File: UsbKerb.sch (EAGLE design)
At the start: 8 parts, among them IC1 XMEGA16A4A

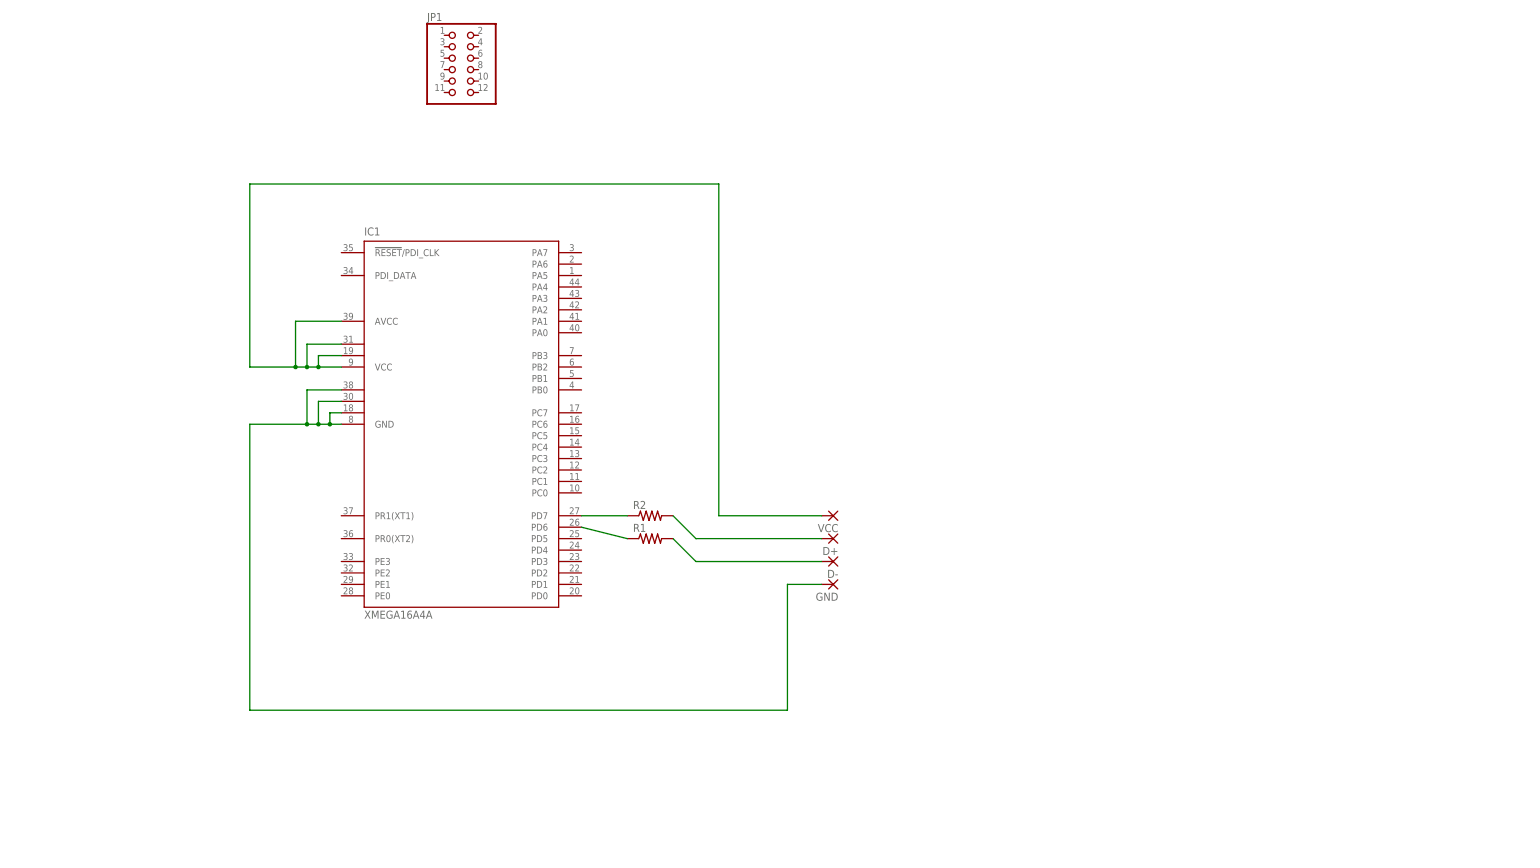
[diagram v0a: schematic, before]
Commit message: more footprints added
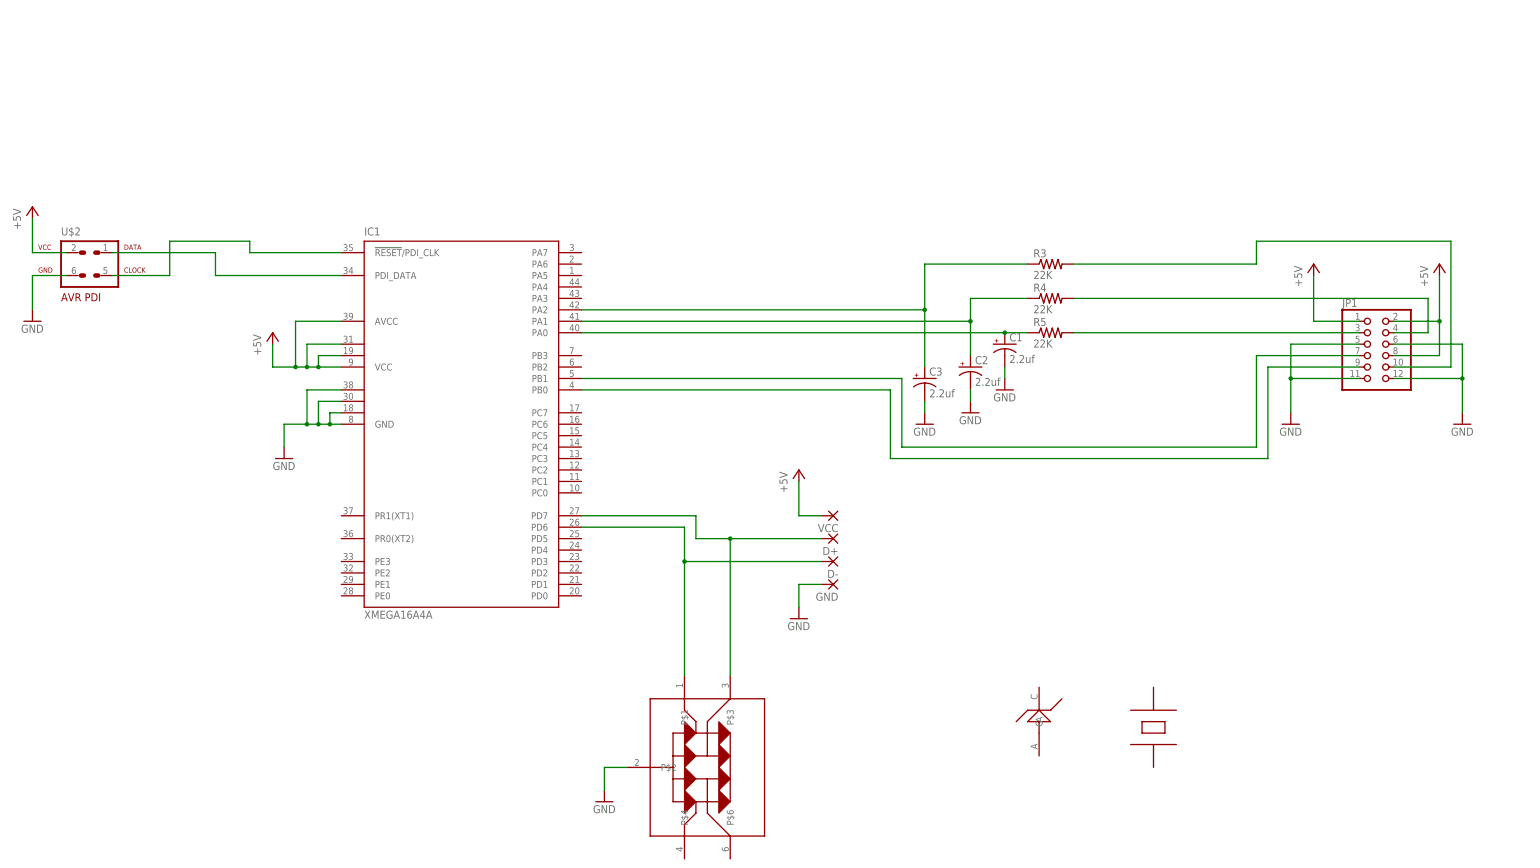
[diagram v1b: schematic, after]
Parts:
- removed R1, R2: (no value), resistor:R-US_R0805W
- added C1, C2, C3: 2.2uf, resistor:CPOL-USB
- added R3, R4, R5: 22K, resistor:R-US_R0805W
- added U$1: PUSB2X4Y, usb:PUSB2X4Y
- added U$2: AVR-PDIVERT, avr-7:AVR-PDIVERT
- added U$3: TVS, usb:TVS
- added U$4: 12MHZ, usb:12MHZ
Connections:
- new net +5V: IC1.AVCC, IC1.VCC, IC1.VCC1, IC1.VCC2, JP1.1, JP1.2, JP1.8, U$2.2, VCC.P
- new net GND: C1.-, C2.-, C3.-, GND.P, IC1.GND, IC1.GND1, IC1.GND2, IC1.GND3, JP1.11, JP1.12, JP1.5, JP1.6, U$1.P$2, U$2.6
- new net N$10: JP1.3, R5.2
- new net N$11: IC1.PB0, JP1.9
- new net N$12: IC1.PB1, JP1.7
- new net N$6: C3.+, IC1.PA2, R3.1
- new net N$7: IC1.!RESET!/PDI_CLK, U$2.5
- new net N$9: JP1.4, R4.2
- net N$1: now also C1.+, IC1.PA0, R5.1; no longer IC1.PD6, R1.1
- net N$2: now also D+.P, U$1.P$3; no longer R2.1
- net N$3: now also IC1.PDI_DATA, U$2.1; no longer D+.P, R2.2
- net N$4: now also IC1.PD6, U$1.P$1; no longer R1.2
- net N$5: now also C2.+, IC1.PA1, R4.1; no longer IC1.AVCC, IC1.VCC, IC1.VCC1, IC1.VCC2, VCC.P
- net N$8: now also JP1.10, R3.2; no longer GND.P, IC1.GND, IC1.GND1, IC1.GND2, IC1.GND3
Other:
- moved on the sheet: JP1

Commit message: Replaced out of stock tvs foot print
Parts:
- U$1: value PUSB2X4Y -> 3.3TVS; device usb:PUSB2X4Y -> usb:3.3TVS
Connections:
- new net N$13: IC1.PR1(XT1), U$4.P$1
- new net N$14: IC1.PR0(XT2), U$4.P$2
- net +5V: now also U$1.VCC, U$3.C
- net GND: now also U$1.GND, U$3.A; no longer U$1.P$2
- net N$2: now also U$1.2; no longer U$1.P$3
- net N$4: now also U$1.1; no longer U$1.P$1
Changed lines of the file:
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@@
 <?xml version="1.0" encoding="utf-8"?>
 <!DOCTYPE eagle SYSTEM "eagle.dtd">
-<eagle version="7.1.0">
+<eagle version="7.2.0">
 <drawing>
 <settings>
@@
 <part name="C2" library="resistor" deviceset="CPOL-US" device="B" value="2.2uf"/>
 <part name="C3" library="resistor" deviceset="CPOL-US" device="B" value="2.2uf"/>
-<part name="U$1" library="usb" deviceset="PUSB2X4Y" device=""/>
 <part name="GND9" library="supply1" deviceset="GND" device=""/>
 <part name="U$2" library="avr-7" deviceset="AVR-PDI" device="VERT"/>
 <part name="U$3" library="usb" deviceset="TVS" device=""/>
 <part name="U$4" library="usb" deviceset="12MHZ" device=""/>
+<part name="U$1" library="usb" deviceset="3.3TVS" device=""/>
+<part name="P+6" library="supply1" deviceset="+5V" device=""/>
+<part name="P+7" library="supply1" deviceset="+5V" device=""/>
+<part name="GND10" library="supply1" deviceset="GND" device=""/>
 </parts>
 <sheets>
@@
 <instance part="C2" gate="G$1" x="180.34" y="63.5"/>
 <instance part="C3" gate="G$1" x="170.18" y="60.96"/>
-<instance part="U$1" gate="G$1" x="121.92" y="-25.4"/>
-<instance part="GND9" gate="1" x="99.06" y="-33.02"/>
+<instance part="GND9" gate="1" x="81.28" y="-33.02"/>
 <instance part="U$2" gate="G$1" x="-15.24" y="86.36"/>
 <instance part="U$3" gate="G$1" x="195.58" y="-15.24"/>
-<instance part="U$4" gate="G$1" x="220.98" y="-15.24" rot="R90"/>
+<instance part="U$4" gate="G$1" x="7.62" y="30.48" rot="R90"/>
+<instance part="U$1" gate="G$1" x="99.06" y="-22.86"/>
+<instance part="P+6" gate="1" x="81.28" y="-12.7"/>
+<instance part="P+7" gate="1" x="195.58" y="-2.54"/>
+<instance part="GND10" gate="1" x="195.58" y="-27.94"/>
 </instances>
 <busses>
@@
 <wire x1="119.38" y1="30.48" x2="119.38" y2="25.4" width="0.1524" layer="91"/>
 <wire x1="93.98" y1="30.48" x2="119.38" y2="30.48" width="0.1524" layer="91"/>
-<pinref part="U$1" gate="G$1" pin="P$3"/>
-<wire x1="127" y1="-5.08" x2="127" y2="25.4" width="0.1524" layer="91"/>
+<wire x1="127" y1="-20.32" x2="127" y2="25.4" width="0.1524" layer="91"/>
 <junction x="127" y="25.4"/>
+<pinref part="U$1" gate="G$1" pin="2"/>
+<wire x1="127" y1="-20.32" x2="111.76" y2="-20.32" width="0.1524" layer="91"/>
 </segment>
 </net>
@@
 <pinref part="IC1" gate="G$1" pin="PD6"/>
 <wire x1="116.84" y1="27.94" x2="93.98" y2="27.94" width="0.1524" layer="91"/>
-<pinref part="U$1" gate="G$1" pin="P$1"/>
-<wire x1="116.84" y1="-5.08" x2="116.84" y2="20.32" width="0.1524" layer="91"/>
+<wire x1="116.84" y1="-15.24" x2="116.84" y2="20.32" width="0.1524" layer="91"/>
 <junction x="116.84" y="20.32"/>
+<pinref part="U$1" gate="G$1" pin="1"/>
+<wire x1="116.84" y1="-15.24" x2="111.76" y2="-15.24" width="0.1524" layer="91"/>
 </segment>
 </net>
@@
 </segment>
 <segment>
-<pinref part="U$1" gate="G$1" pin="P$2"/>
 <pinref part="GND9" gate="1" pin="GND"/>
-<wire x1="104.14" y1="-25.4" x2="99.06" y2="-25.4" width="0.1524" layer="91"/>
-<wire x1="99.06" y1="-25.4" x2="99.06" y2="-30.48" width="0.1524" layer="91"/>
+<wire x1="86.36" y1="-25.4" x2="81.28" y2="-25.4" width="0.1524" layer="91"/>
+<wire x1="81.28" y1="-25.4" x2="81.28" y2="-30.48" width="0.1524" layer="91"/>
+<pinref part="U$1" gate="G$1" pin="GND"/>
+</segment>
+<segment>
+<pinref part="U$3" gate="G$1" pin="A"/>
+<pinref part="GND10" gate="1" pin="GND"/>
+<wire x1="195.58" y1="-22.86" x2="195.58" y2="-25.4" width="0.1524" layer="91"/>
 </segment>
 </net>
@@
 <wire x1="142.24" y1="30.48" x2="142.24" y2="38.1" width="0.1524" layer="91"/>
 </segment>
+<segment>
+<pinref part="U$1" gate="G$1" pin="VCC"/>
+<pinref part="P+6" gate="1" pin="+5V"/>
+<wire x1="86.36" y1="-20.32" x2="81.28" y2="-20.32" width="0.1524" layer="91"/>
+<wire x1="81.28" y1="-20.32" x2="81.28" y2="-15.24" width="0.1524" layer="91"/>
+</segment>
+<segment>
+<pinref part="U$3" gate="G$1" pin="C"/>
+<pinref part="P+7" gate="1" pin="+5V"/>
+<wire x1="195.58" y1="-7.62" x2="195.58" y2="-5.08" width="0.1524" layer="91"/>
+</segment>
 </net>
 <net name="N$1" class="0">
@@
 </segment>
 </net>
+<net name="N$13" class="0">
+<segment>
+<pinref part="U$4" gate="G$1" pin="P$1"/>
+<wire x1="7.62" y1="38.1" x2="22.86" y2="38.1" width="0.1524" layer="91"/>
+<wire x1="22.86" y1="38.1" x2="22.86" y2="30.48" width="0.1524" layer="91"/>
+<pinref part="IC1" gate="G$1" pin="PR1(XT1)"/>
+<wire x1="22.86" y1="30.48" x2="40.64" y2="30.48" width="0.1524" layer="91"/>
+</segment>
+</net>
+<net name="N$14" class="0">
+<segment>
+<pinref part="U$4" gate="G$1" pin="P$2"/>
+<wire x1="7.62" y1="20.32" x2="22.86" y2="20.32" width="0.1524" layer="91"/>
+<wire x1="22.86" y1="20.32" x2="22.86" y2="25.4" width="0.1524" layer="91"/>
+<pinref part="IC1" gate="G$1" pin="PR0(XT2)"/>
+<wire x1="22.86" y1="25.4" x2="40.64" y2="25.4" width="0.1524" layer="91"/>
+</segment>
+</net>

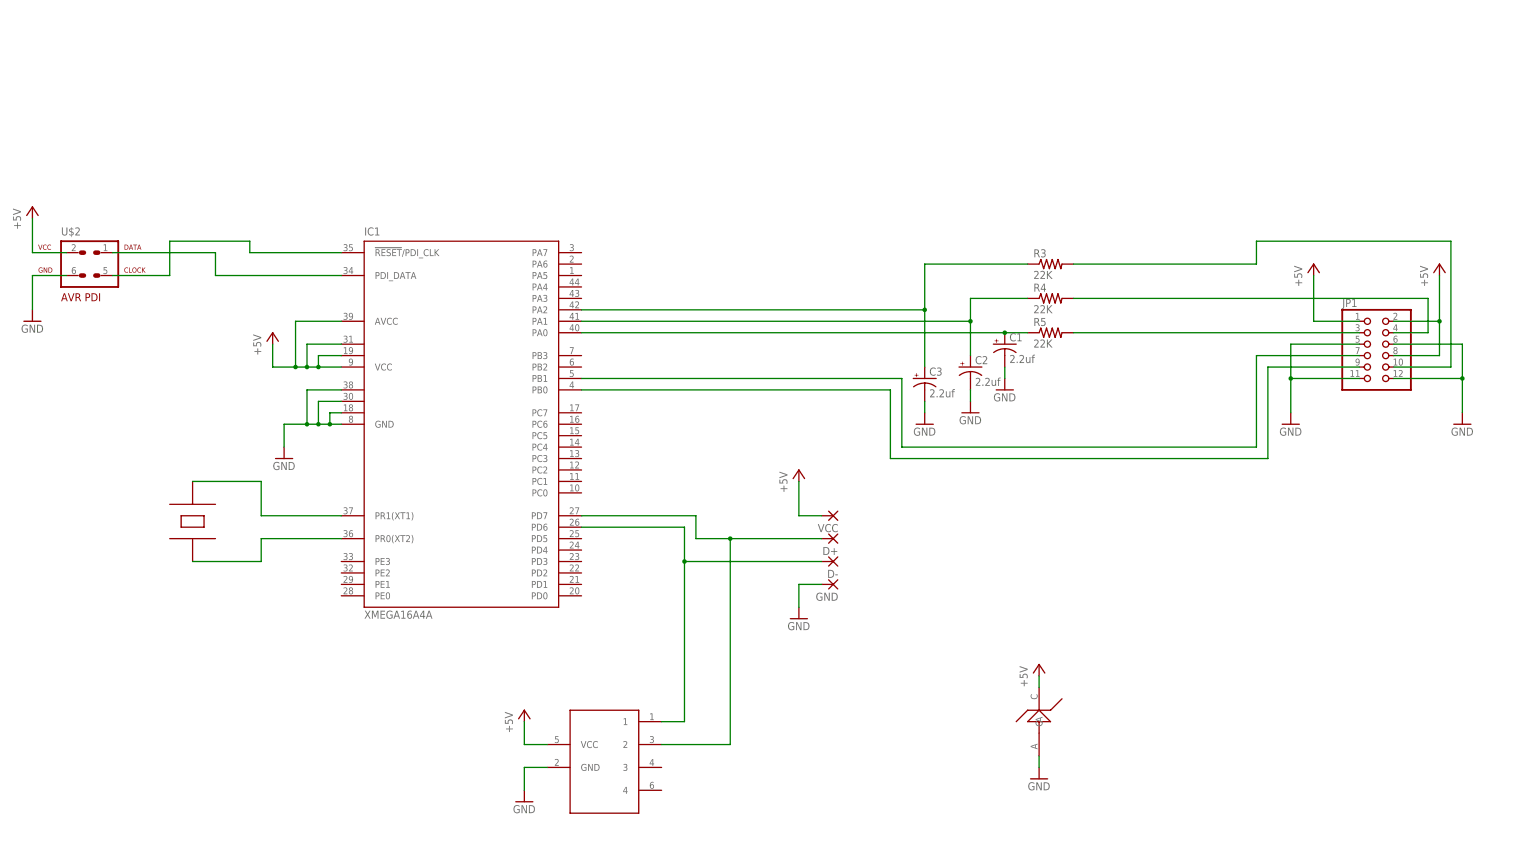
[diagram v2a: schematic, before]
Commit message: fixed power rails
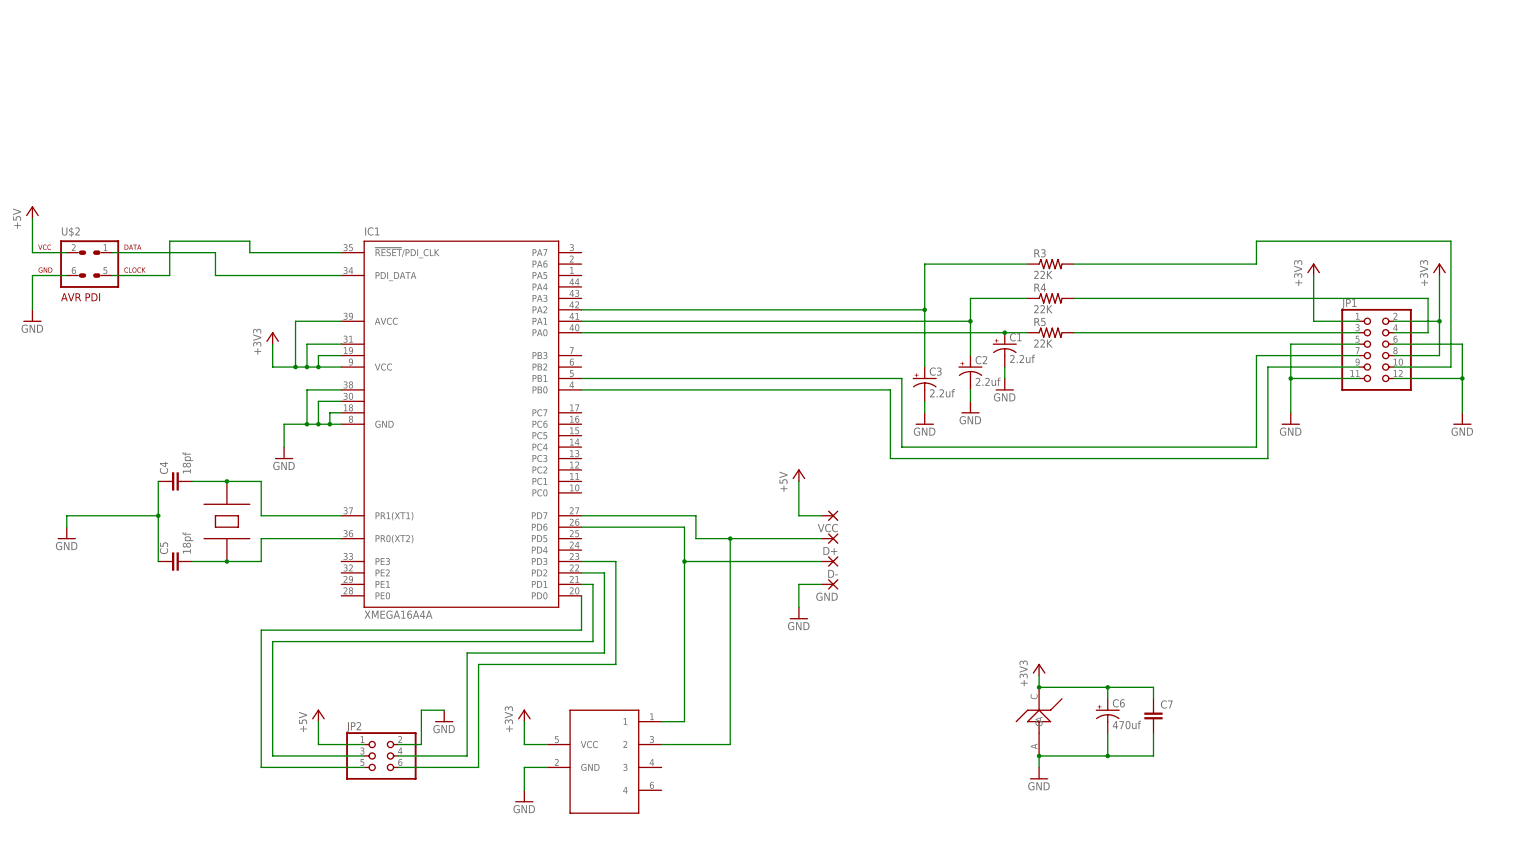
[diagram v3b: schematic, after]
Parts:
- added C4, C5: 18pf, rcl:C-EUC0805K
- added C6: 470uf, rcl:CPOL-USG
- added C7: (no value), rcl:C-EUC0805K
- added JP2: (no value), pinhead:PINHD-2X3
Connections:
- new net +3V3: C6.+, C7.1, IC1.AVCC, IC1.VCC, IC1.VCC1, IC1.VCC2, JP1.1, JP1.2, JP1.8, U$1.VCC, U$3.C
- new net N$15: JP2.3
- new net N$16: IC1.PD2, JP2.4
- new net N$17: IC1.PD0, JP2.5
- new net N$18: IC1.PD1
- new net N$19: IC1.PD3, JP2.6
- net +5V: now also JP2.1; no longer IC1.AVCC, IC1.VCC, IC1.VCC1, IC1.VCC2, JP1.1, JP1.2, JP1.8, U$1.VCC, U$3.C
- net GND: now also C4.1, C5.1, C6.-, C7.2, JP2.2
- net N$13: now also C4.2
- net N$14: now also C5.2
